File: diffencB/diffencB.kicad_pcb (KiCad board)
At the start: 4 copper layers, 40 x 22 mm, 13 parts, among them J1 RJ45_Shielded, U1 SN65LVDT41

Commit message: diffencB: v1
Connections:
- J1 pad 4: Net-(U1-2Z) -> Net-(U1-5A)
- J1 pad 5: Net-(U1-5A) -> Net-(U1-5B)
- J1 pad 6: Net-(U1-5B) -> Net-(U1-2Z)
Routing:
- net Net-(U1-5B): track 11.4 -> 9.72 mm
- net Net-(U1-5A): track 8.48 -> 7.97 mm
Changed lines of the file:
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@@
       (net 6 "Net-(U1-2Y)") (pintype "passive") (thermal_bridge_angle 45))
     (pad "4" smd roundrect (at -0.635 -10.9 270) (size 0.8 4) (layers "F.Cu" "F.Paste" "F.Mask") (roundrect_rratio 0.25)
+      (net 8 "Net-(U1-5A)") (pintype "passive") (thermal_bridge_angle 45))
+    (pad "5" smd roundrect (at 0.635 -10.9 270) (size 0.8 4) (layers "F.Cu" "F.Paste" "F.Mask") (roundrect_rratio 0.25)
+      (net 9 "Net-(U1-5B)") (pintype "passive") (thermal_bridge_angle 45))
+    (pad "6" smd roundrect (at 1.905 -10.9 270) (size 0.8 4) (layers "F.Cu" "F.Paste" "F.Mask") (roundrect_rratio 0.25)
       (net 7 "Net-(U1-2Z)") (pintype "passive") (thermal_bridge_angle 45))
-    (pad "5" smd roundrect (at 0.635 -10.9 270) (size 0.8 4) (layers "F.Cu" "F.Paste" "F.Mask") (roundrect_rratio 0.25)
-      (net 8 "Net-(U1-5A)") (pintype "passive") (thermal_bridge_angle 45))
-    (pad "6" smd roundrect (at 1.905 -10.9 270) (size 0.8 4) (layers "F.Cu" "F.Paste" "F.Mask") (roundrect_rratio 0.25)
-      (net 9 "Net-(U1-5B)") (pintype "passive") (thermal_bridge_angle 45))
     (pad "7" smd roundrect (at 3.175 -10.9 270) (size 0.8 4) (layers "F.Cu" "F.Paste" "F.Mask") (roundrect_rratio 0.25)
       (net 1 "+3V3") (pintype "passive") (thermal_bridge_angle 45))
@@
   (segment (start 75 64.5) (end 77.8255 64.5) (width 0.25) (layer "B.Cu") (net 6))
   (segment (start 74.512299 64.012299) (end 75 64.5) (width 0.25) (layer "B.Cu") (net 6))
+  (segment (start 74.314554 67.218777) (end 71.988777 67.218777) (width 0.25) (layer "F.Cu") (net 7))
   (segment (start 77.025 65.975) (end 76.1375 65.975) (width 0.25) (layer "F.Cu") (net 7))
   (segment (start 77.711779 65.288221) (end 77.025 65.975) (width 0.25) (layer "F.Cu") (net 7))
-  (segment (start 73.147462 64.365) (end 71.675 64.365) (width 0.25) (layer "F.Cu") (net 7))
-  (segment (start 73.800589 65.018127) (end 73.147462 64.365) (width 0.25) (layer "F.Cu") (net 7))
-  (segment (start 74.493595 65.018127) (end 73.800589 65.018127) (width 0.25) (layer "F.Cu") (net 7))
+  (segment (start 74.500533 67.032798) (end 74.314554 67.218777) (width 0.25) (layer "F.Cu") (net 7))
+  (segment (start 71.988777 67.218777) (end 71.675 66.905) (width 0.25) (layer "F.Cu") (net 7))
   (segment (start 77.788222 65.288221) (end 77.711779 65.288221) (width 0.25) (layer "F.Cu") (net 7))
   (via (at 77.788222 65.288221) (size 0.8) (drill 0.4) (layers "F.Cu" "B.Cu") (net 7))
-  (via (at 74.493595 65.018127) (size 0.8) (drill 0.4) (layers "F.Cu" "B.Cu") (net 7))
-  (segment (start 75.55018 66.074712) (end 77.425288 66.074712) (width 0.25) (layer "B.Cu") (net 7))
-  (segment (start 74.493595 65.018127) (end 75.55018 66.074712) (width 0.25) (layer "B.Cu") (net 7))
-  (segment (start 77.788222 65.711778) (end 77.788222 65.288221) (width 0.25) (layer "B.Cu") (net 7))
-  (segment (start 77.425288 66.074712) (end 77.788222 65.711778) (width 0.25) (layer "B.Cu") (net 7))
+  (via (at 74.500533 67.032798) (size 0.8) (drill 0.4) (layers "F.Cu" "B.Cu") (net 7))
+  (segment (start 76 65.75) (end 74.717202 67.032798) (width 0.25) (layer "B.Cu") (net 7))
+  (segment (start 77.788222 65.288221) (end 77.326443 65.75) (width 0.25) (layer "B.Cu") (net 7))
+  (segment (start 74.717202 67.032798) (end 74.500533 67.032798) (width 0.25) (layer "B.Cu") (net 7))
+  (segment (start 77.326443 65.75) (end 76 65.75) (width 0.25) (layer "B.Cu") (net 7))
   (segment (start 74.775 62.725) (end 76.1375 62.725) (width 0.25) (layer "F.Cu") (net 8))
+  (segment (start 73.147462 64.365) (end 71.675 64.365) (width 0.25) (layer "F.Cu") (net 8))
+  (segment (start 73.800589 65.018127) (end 73.147462 64.365) (width 0.25) (layer "F.Cu") (net 8))
   (segment (start 74.5 63) (end 74.775 62.725) (width 0.25) (layer "F.Cu") (net 8))
-  (segment (start 74.08587 65.635) (end 71.675 65.635) (width 0.25) (layer "F.Cu") (net 8))
-  (segment (start 74.484297 66.033427) (end 74.08587 65.635) (width 0.25) (layer "F.Cu") (net 8))
-  (via (at 74.484297 66.033427) (size 0.8) (drill 0.4) (layers "F.Cu" "B.Cu") (net 8))
+  (segment (start 74.493595 65.018127) (end 73.800589 65.018127) (width 0.25) (layer "F.Cu") (net 8))
   (via (at 74.5 63) (size 0.8) (drill 0.4) (layers "F.Cu" "B.Cu") (net 8))
-  (segment (start 74.484297 66.033427) (end 73.6255 65.17463) (width 0.25) (layer "B.Cu") (net 8))
-  (segment (start 73.6255 65.17463) (end 73.6255 63.8745) (width 0.25) (layer "B.Cu") (net 8))
-  (segment (start 73.6255 63.8745) (end 74.5 63) (width 0.25) (layer "B.Cu") (net 8))
-  (segment (start 74.314554 67.218777) (end 71.988777 67.218777) (width 0.25) (layer "F.Cu") (net 9))
+  (via (at 74.493595 65.018127) (size 0.8) (drill 0.4) (layers "F.Cu" "B.Cu") (net 8))
+  (segment (start 74.105393 65.018127) (end 73.7 64.612734) (width 0.25) (layer "B.Cu") (net 8))
+  (segment (start 73.7 64.612734) (end 73.7 63.411091) (width 0.25) (layer "B.Cu") (net 8))
+  (segment (start 74.111091 63) (end 74.5 63) (width 0.25) (layer "B.Cu") (net 8))
+  (segment (start 73.7 63.411091) (end 74.111091 63) (width 0.25) (layer "B.Cu") (net 8))
+  (segment (start 74.493595 65.018127) (end 74.105393 65.018127) (width 0.25) (layer "B.Cu") (net 8))
   (segment (start 76.0625 62) (end 76.1375 62.075) (width 0.25) (layer "F.Cu") (net 9))
-  (segment (start 74.500533 67.032798) (end 74.314554 67.218777) (width 0.25) (layer "F.Cu") (net 9))
-  (segment (start 71.988777 67.218777) (end 71.675 66.905) (width 0.25) (layer "F.Cu") (net 9))
+  (segment (start 74.08587 65.635) (end 71.675 65.635) (width 0.25) (layer "F.Cu") (net 9))
+  (segment (start 74.484297 66.033427) (end 74.08587 65.635) (width 0.25) (layer "F.Cu") (net 9))
   (segment (start 74.5 62) (end 76.0625 62) (width 0.25) (layer "F.Cu") (net 9))
+  (via (at 74.484297 66.033427) (size 0.8) (drill 0.4) (layers "F.Cu" "B.Cu") (net 9))
   (via (at 74.5 62) (size 0.8) (drill 0.4) (layers "F.Cu" "B.Cu") (net 9))
-  (via (at 74.500533 67.032798) (size 0.8) (drill 0.4) (layers "F.Cu" "B.Cu") (net 9))
-  (segment (start 73.1755 63.099) (end 74.2745 62) (width 0.25) (layer "B.Cu") (net 9))
-  (segment (start 74.2745 62) (end 74.5 62) (width 0.25) (layer "B.Cu") (net 9))
-  (segment (start 73.1755 66.448488) (end 73.1755 63.099) (width 0.25) (layer "B.Cu") (net 9))
-  (segment (start 73.75981 67.032798) (end 73.1755 66.448488) (width 0.25) (layer "B.Cu") (net 9))
-  (segment (start 74.500533 67.032798) (end 73.75981 67.032798) (width 0.25) (layer "B.Cu") (net 9))
+  (segment (start 74.474695 62) (end 74.5 62) (width 0.25) (layer "B.Cu") (net 9))
+  (segment (start 73.25 64.79913) (end 73.25 63.224695) (width 0.25) (layer "B.Cu") (net 9))
+  (segment (start 73.25 63.224695) (end 74.474695 62) (width 0.25) (layer "B.Cu") (net 9))
+  (segment (start 74.484297 66.033427) (end 73.25 64.79913) (width 0.25) (layer "B.Cu") (net 9))
   (segment (start 84 69) (end 82.925 67.925) (width 0.25) (layer "F.Cu") (net 16))
   (segment (start 82.925 67.925) (end 81.8625 67.925) (width 0.25) (layer "F.Cu") (net 16))

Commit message: diffencb: silk
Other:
- board text added: "DiffEncB V1"
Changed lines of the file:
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@@
   (gr_line (start 51 74) (end 51 56)
     (stroke (width 0.1) (type default)) (layer "Edge.Cuts"))
+  (gr_text "DiffEncB V1" (at 60.5 75.5) (layer "F.SilkS")
+    (effects (font (size 1.5 1.5) (thickness 0.3) bold) (justify left bottom))
+  )
   (dimension (type aligned) (layer "Eco1.User")
     (pts (xy 51 54) (xy 51 76))

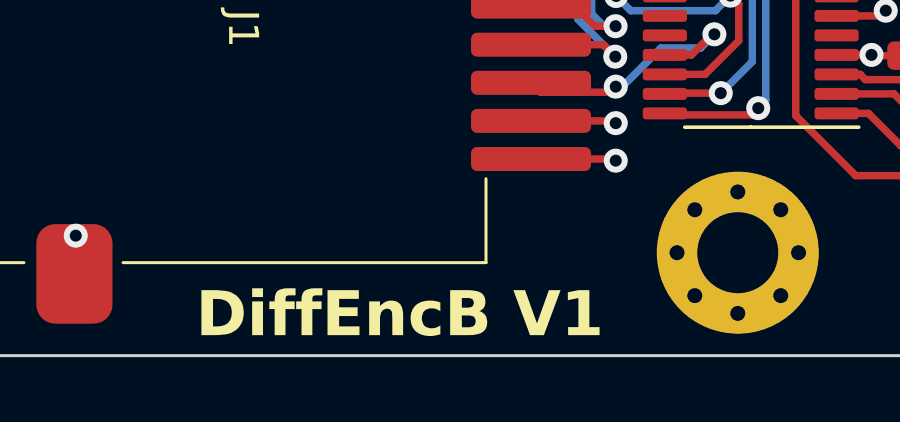
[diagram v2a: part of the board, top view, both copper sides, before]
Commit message: diffencb: V1 -> v1
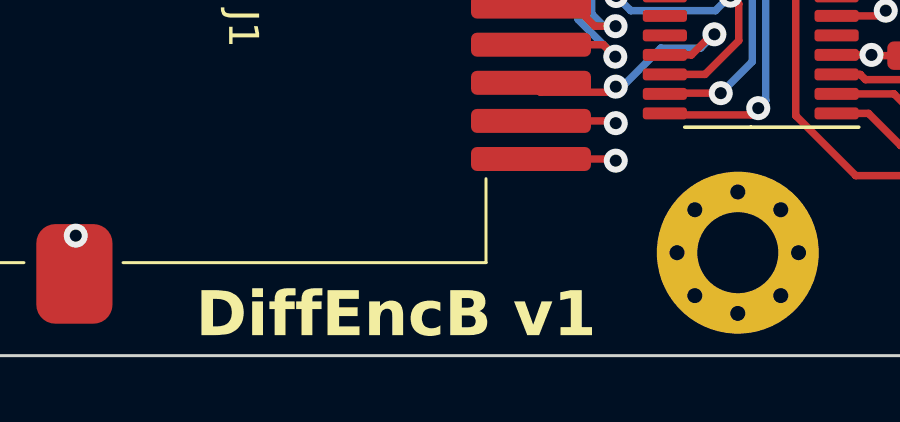
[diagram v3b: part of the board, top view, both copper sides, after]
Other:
- board text added: "DiffEncB v1"
- board text removed: "DiffEncB V1"
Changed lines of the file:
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@@
   (gr_line (start 51 74) (end 51 56)
     (stroke (width 0.1) (type default)) (layer "Edge.Cuts"))
-  (gr_text "DiffEncB V1" (at 60.5 75.5) (layer "F.SilkS")
+  (gr_text "DiffEncB v1" (at 60.5 75.5) (layer "F.SilkS")
     (effects (font (size 1.5 1.5) (thickness 0.3) bold) (justify left bottom))
   )

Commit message: diffencB: diff pairs
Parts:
- moved C5 1.11 mm to (84.0, 66.8), turned to -90 degrees
- moved C4 0.80 mm to (84.0, 62.8), turned to 90 degrees
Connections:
- net Net-(U1-1Y) renamed /LVD1_P
- net Net-(U1-1Z) renamed /LVD1_N
- J1 pad 3: Net-(U1-2Y) -> +3V3
- J1 pad 4: Net-(U1-5A) -> /LVD2_P
- J1 pad 5: Net-(U1-5B) -> /LVD2_N
- J1 pad 6: Net-(U1-2Z) -> GND
- J1 pad 7: +3V3 -> /LVD5_P
- J1 pad 8: GND -> /LVD5_N
- U1 pad 11: Net-(U1-5B) -> /LVD5_N
- U1 pad 12: Net-(U1-5A) -> /LVD5_P
- U1 pad 17: Net-(U1-2Z) -> /LVD2_N
- U1 pad 18: Net-(U1-2Y) -> /LVD2_P
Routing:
- net /LVD5_N: track 0.00 -> 16.9 mm, vias 0 -> 2
- net /LVD5_P: track 0.00 -> 13.8 mm, vias 0 -> 2
- net Net-(U1-2Y): track 12.0 -> 0.00 mm, vias 2 -> 0
- net /LVD2_N: track 0.00 -> 11.0 mm, vias 0 -> 2
- net /LVD2_P: track 0.00 -> 10.6 mm, vias 0 -> 2
- net Net-(U1-5B): track 9.72 -> 0.00 mm, vias 2 -> 0
- net Net-(U1-2Z): track 8.98 -> 0.00 mm, vias 2 -> 0
- net Net-(U1-5A): track 7.97 -> 0.00 mm, vias 2 -> 0
- net /LVD1_N: track 14.9 -> 18.0 mm
- net GND: track 17.0 -> 14.1 mm, vias 9 -> 7
- net +3V3: track 14.5 -> 16.7 mm
- net Net-(CS1-Pin_1): track 9.46 -> 8.87 mm
- added copper zone on B.Cu, net GND
